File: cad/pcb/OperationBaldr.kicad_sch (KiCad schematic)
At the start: 20 parts, among them J1 Conn_01x10_Pin, J2 Conn_01x04_Pin, U4 ULN2003A, U5 ULN2003A, U6 74HC595, U7 74HC595, U8 74HC595, U9 ULN2003A

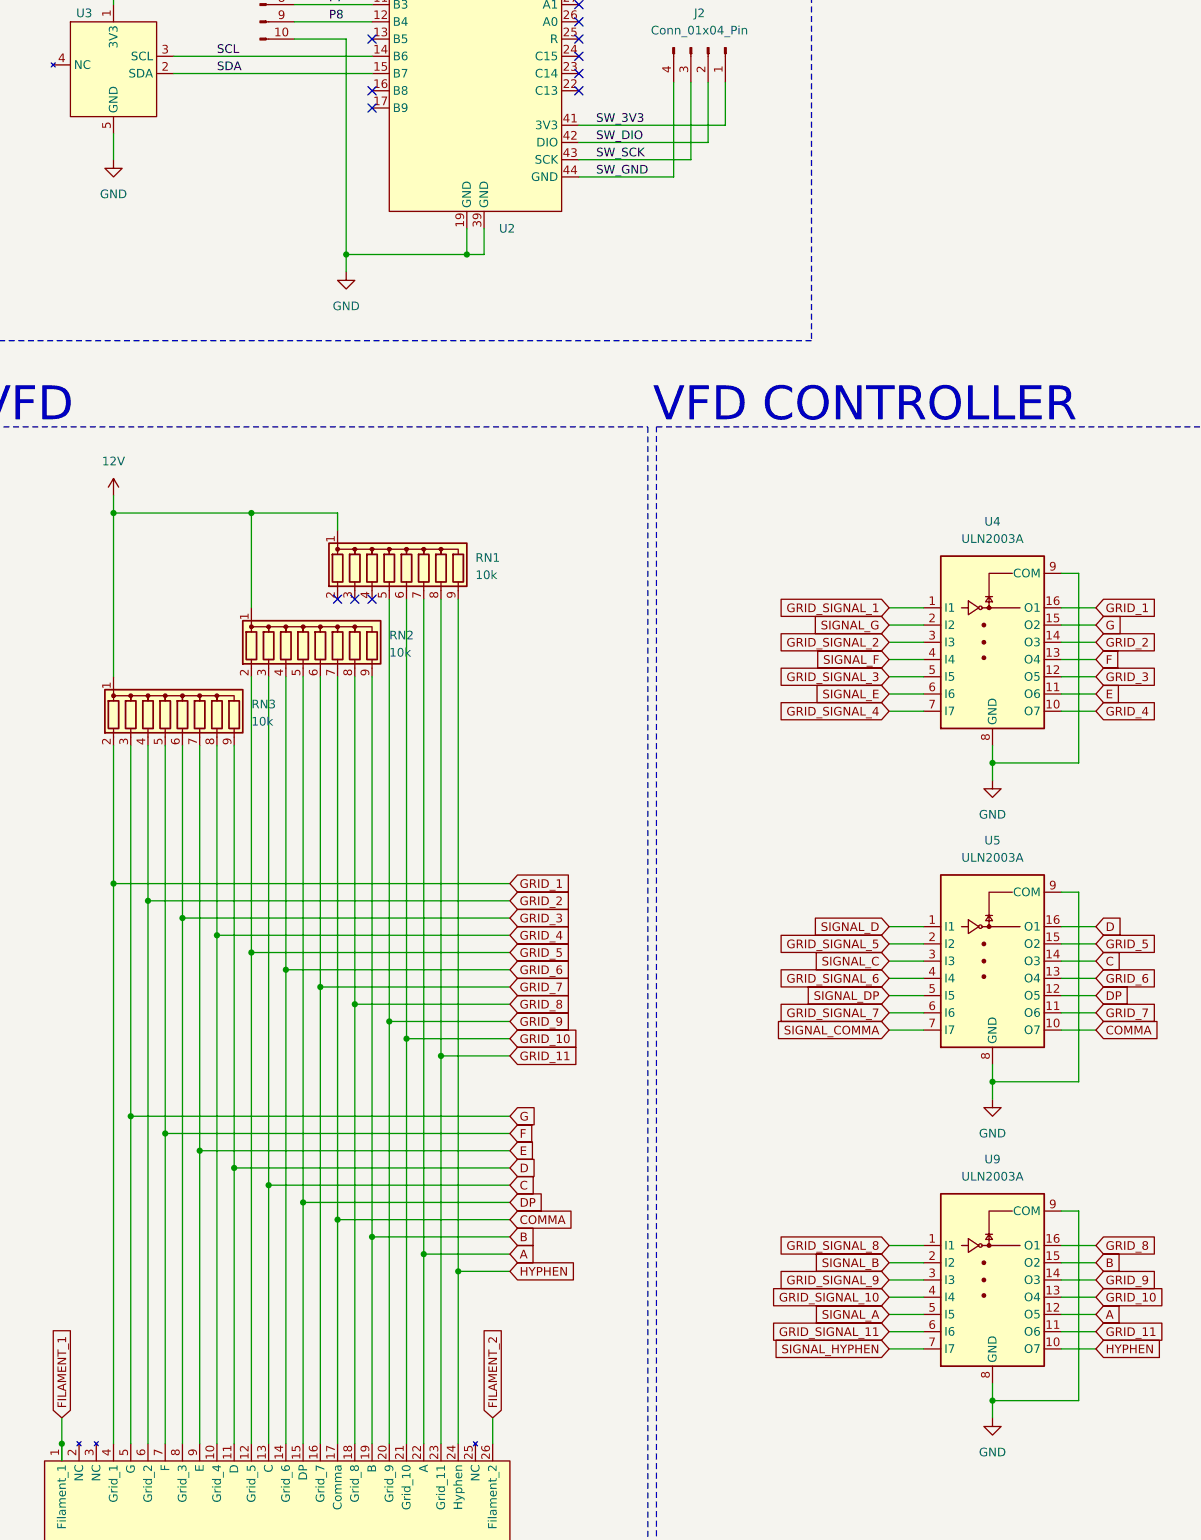
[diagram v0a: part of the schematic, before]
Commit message: Added embedded rust code
Added an embedded rust program to control the device.
Also restructered file hierarchy, and made revisions to schematic/pcb.
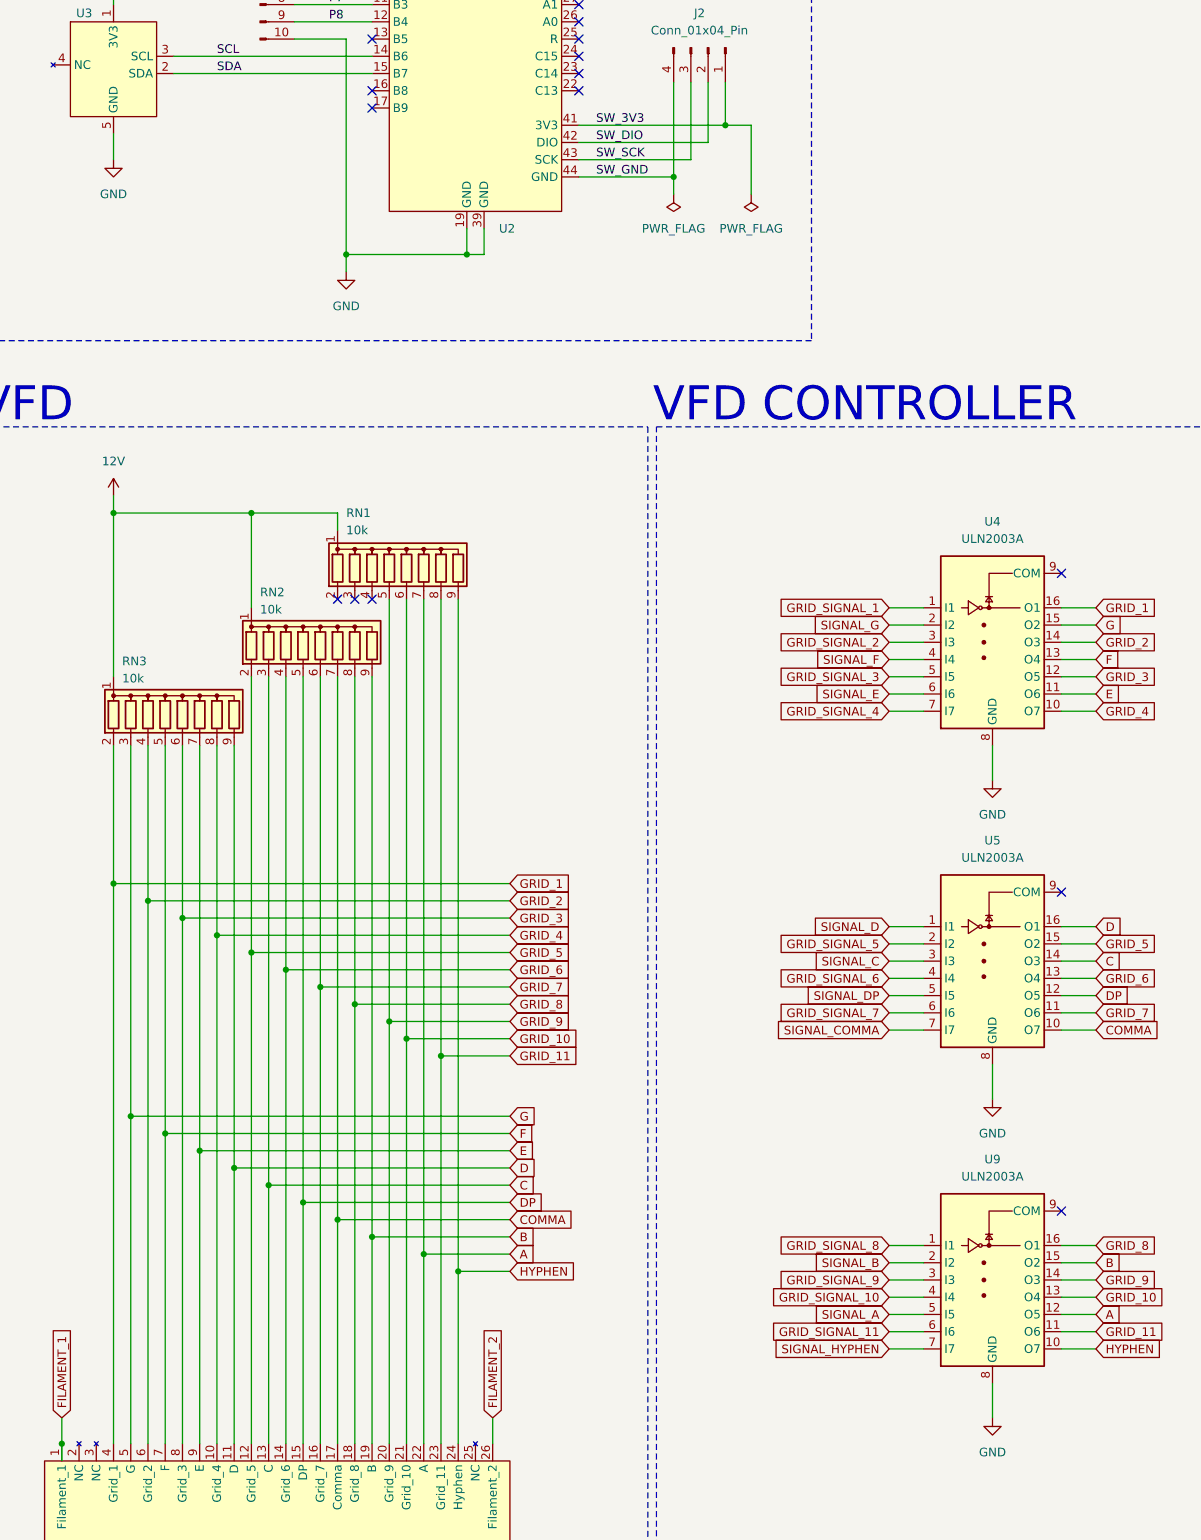
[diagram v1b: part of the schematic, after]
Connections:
- net GND: no longer U4.9 (COM), U5.9 (COM), U9.9 (COM)
- no-connect marks 28 -> 31
